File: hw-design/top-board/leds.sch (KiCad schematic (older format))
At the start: 30 parts

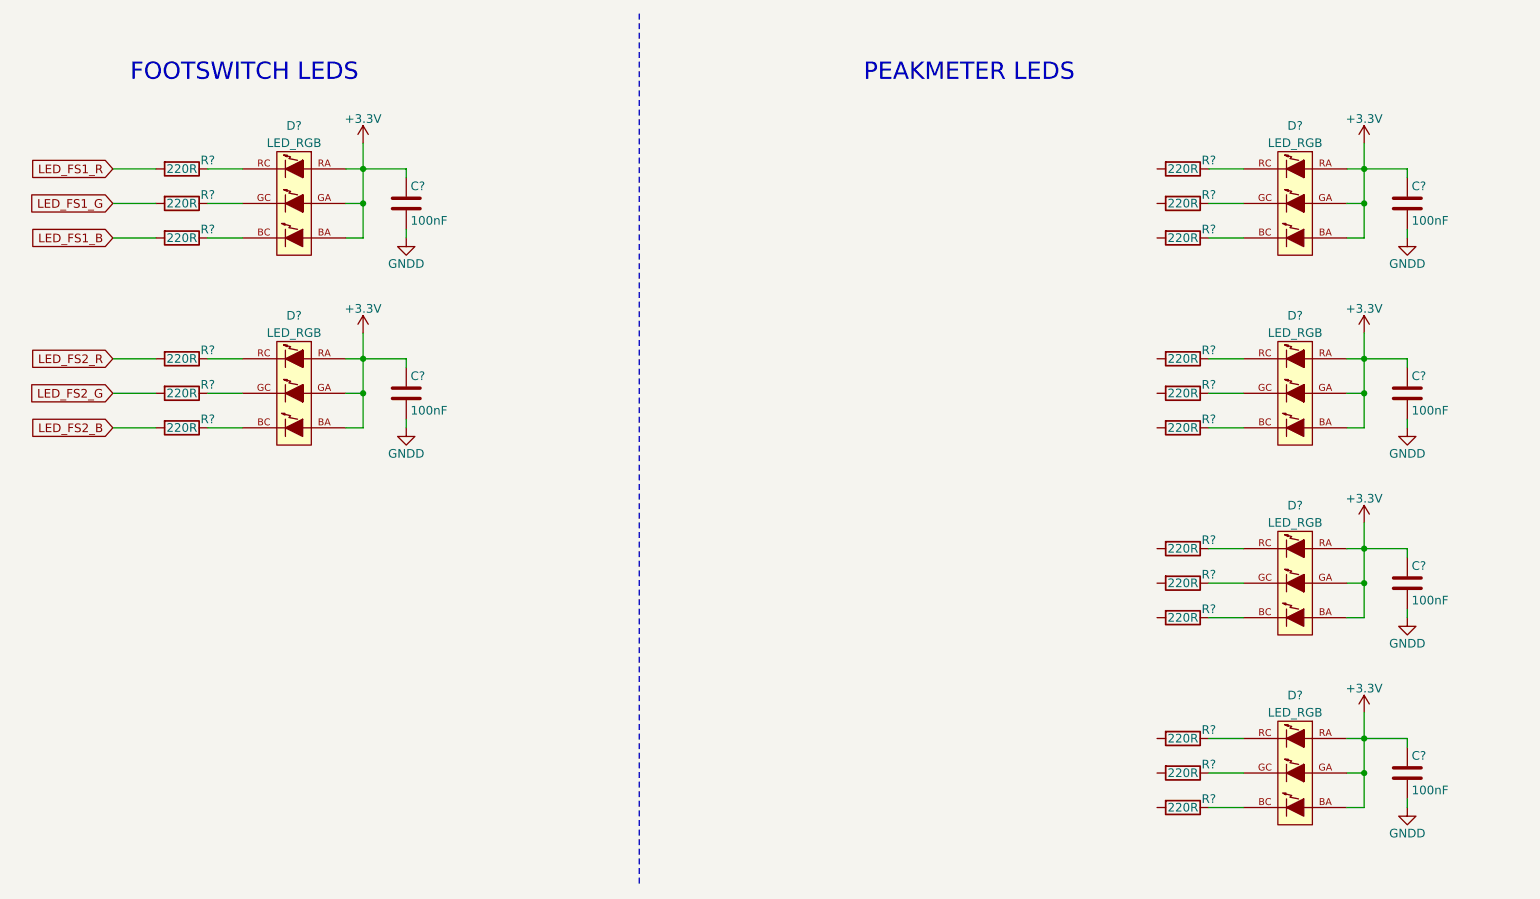
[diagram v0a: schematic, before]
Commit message: sch,top-board: added PCA9685 led driver
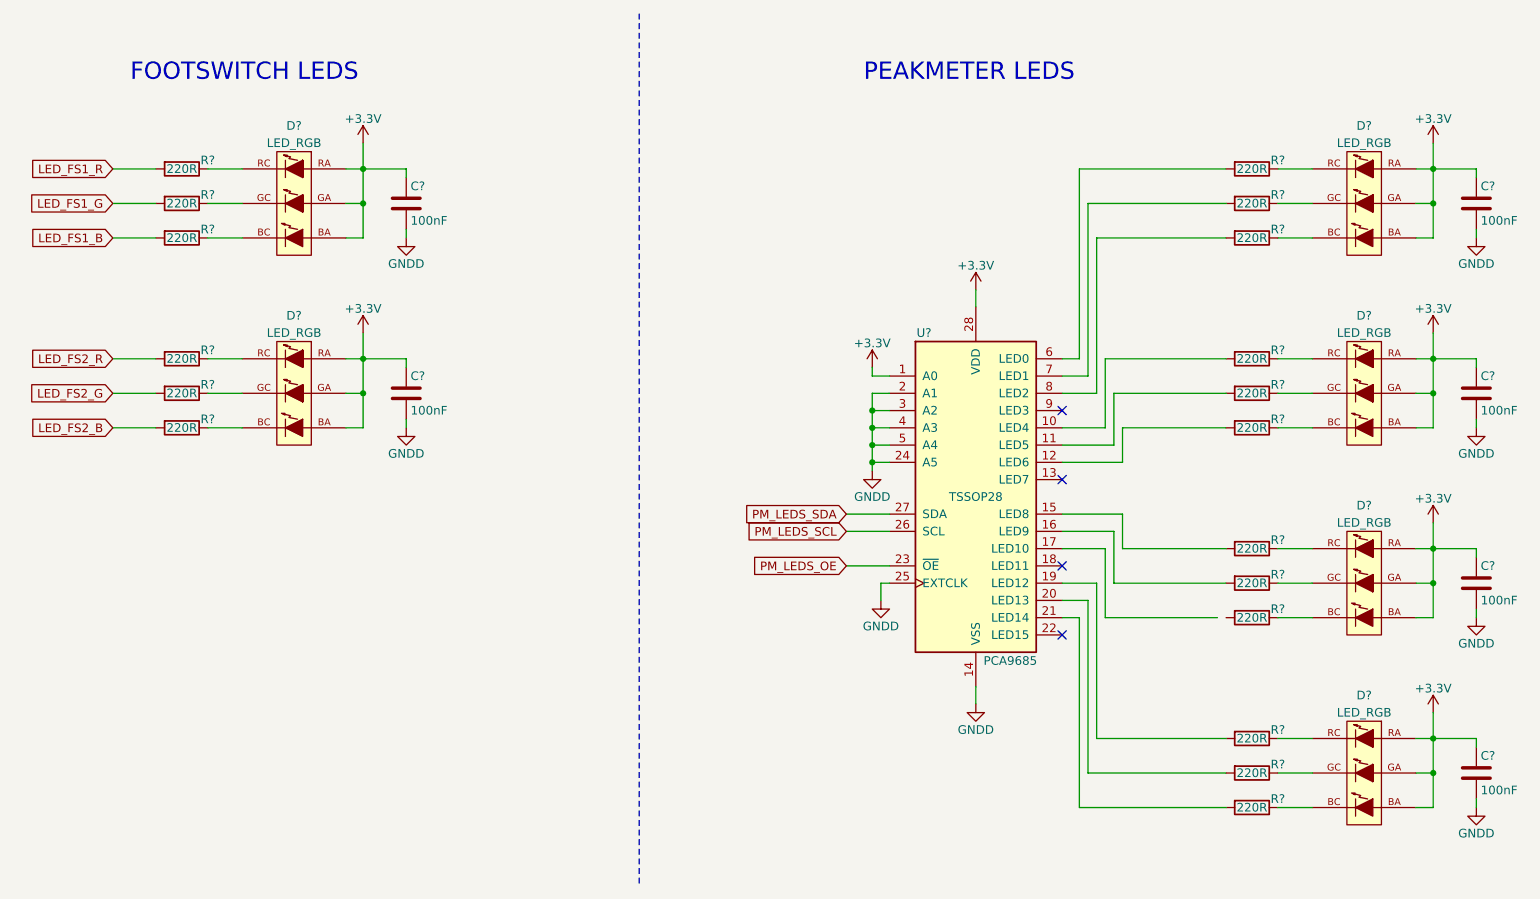
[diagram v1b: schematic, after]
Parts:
- added U?: PCA9685, TSSOP28, symbol PCA9685
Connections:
- net +3V3: now also U?.1 (A0), U?.28 (VDD)
- net GNDD: now also U?.14 (VSS), U?.2 (A1), U?.24 (A5), U?.25 (EXTCLK), U?.3 (A2), U?.4 (A3), U?.5 (A4)
- net at R?.2: now also U?.6 (LED0)
- net at R?.2: now also U?.7 (LED1)
- net at R?.2: now also U?.8 (LED2)
- net at R?.2: now also U?.10 (LED4)
- net at R?.2: now also U?.11 (LED5)
- net at R?.2: now also U?.12 (LED6)
- net at R?.2: now also U?.15 (LED8)
- net at R?.2: now also U?.16 (LED9)
- net at R?.2: now also U?.19 (LED12)
- net at R?.2: now also U?.20 (LED13)
- net at R?.2: now also U?.21 (LED14)
- new net PM_LEDS_OE: U?.23 (~OE~)
- new net PM_LEDS_SCL: U?.26 (SCL)
- new net PM_LEDS_SDA: U?.27 (SDA)
- no-connect marks 0 -> 4
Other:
- moved on the sheet: C?, D?, R?

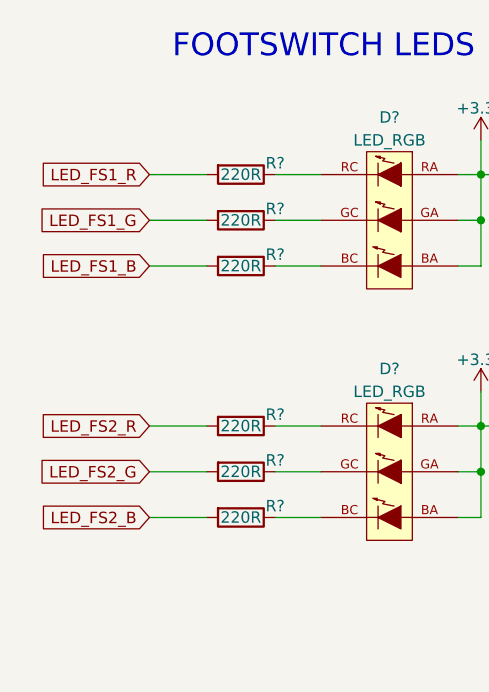
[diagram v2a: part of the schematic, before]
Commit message: sch,top-board: adding uC signals (wip)
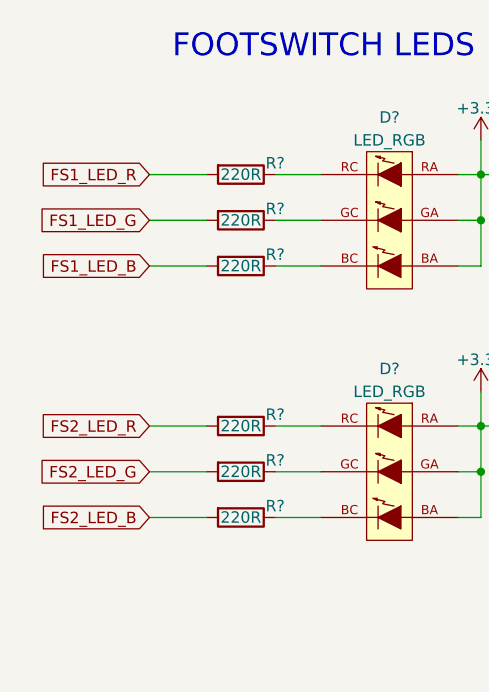
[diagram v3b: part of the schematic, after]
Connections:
- net LED_FS1_B renamed FS1_LED_B
- net LED_FS1_G renamed FS1_LED_G
- net LED_FS1_R renamed FS1_LED_R
- net LED_FS2_B renamed FS2_LED_B
- net LED_FS2_G renamed FS2_LED_G
- net LED_FS2_R renamed FS2_LED_R
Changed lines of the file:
@@
 	1    0    0    -1
 $EndComp
-Text GLabel 1750 1850 0    50   Input ~ 0
-LED_FS1_R
-Text GLabel 1750 2050 0    50   Input ~ 0
-LED_FS1_G
-Text GLabel 1750 2250 0    50   Input ~ 0
-LED_FS1_B
 $Comp
 L LED_RGB D?
@@
 	1    0    0    -1
 $EndComp
-Text GLabel 1750 2950 0    50   Input ~ 0
-LED_FS2_R
-Text GLabel 1750 3150 0    50   Input ~ 0
-LED_FS2_G
-Text GLabel 1750 3350 0    50   Input ~ 0
-LED_FS2_B
 Text Notes 1850 1350 0    100  ~ 0
 FOOTSWITCH LEDS
@@
 NoConn ~ 7250 4550
 NoConn ~ 7250 4150
+Text GLabel 1750 1850 0    50   Input ~ 0
+FS1_LED_R
+Text GLabel 1750 2050 0    50   Input ~ 0
+FS1_LED_G
+Text GLabel 1750 2250 0    50   Input ~ 0
+FS1_LED_B
+Text GLabel 1750 2950 0    50   Input ~ 0
+FS2_LED_R
+Text GLabel 1750 3150 0    50   Input ~ 0
+FS2_LED_G
+Text GLabel 1750 3350 0    50   Input ~ 0
+FS2_LED_B
 $EndSCHEMATC

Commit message: sch,top-board: annotation done
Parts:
- gave numbers to parts that had none: 31

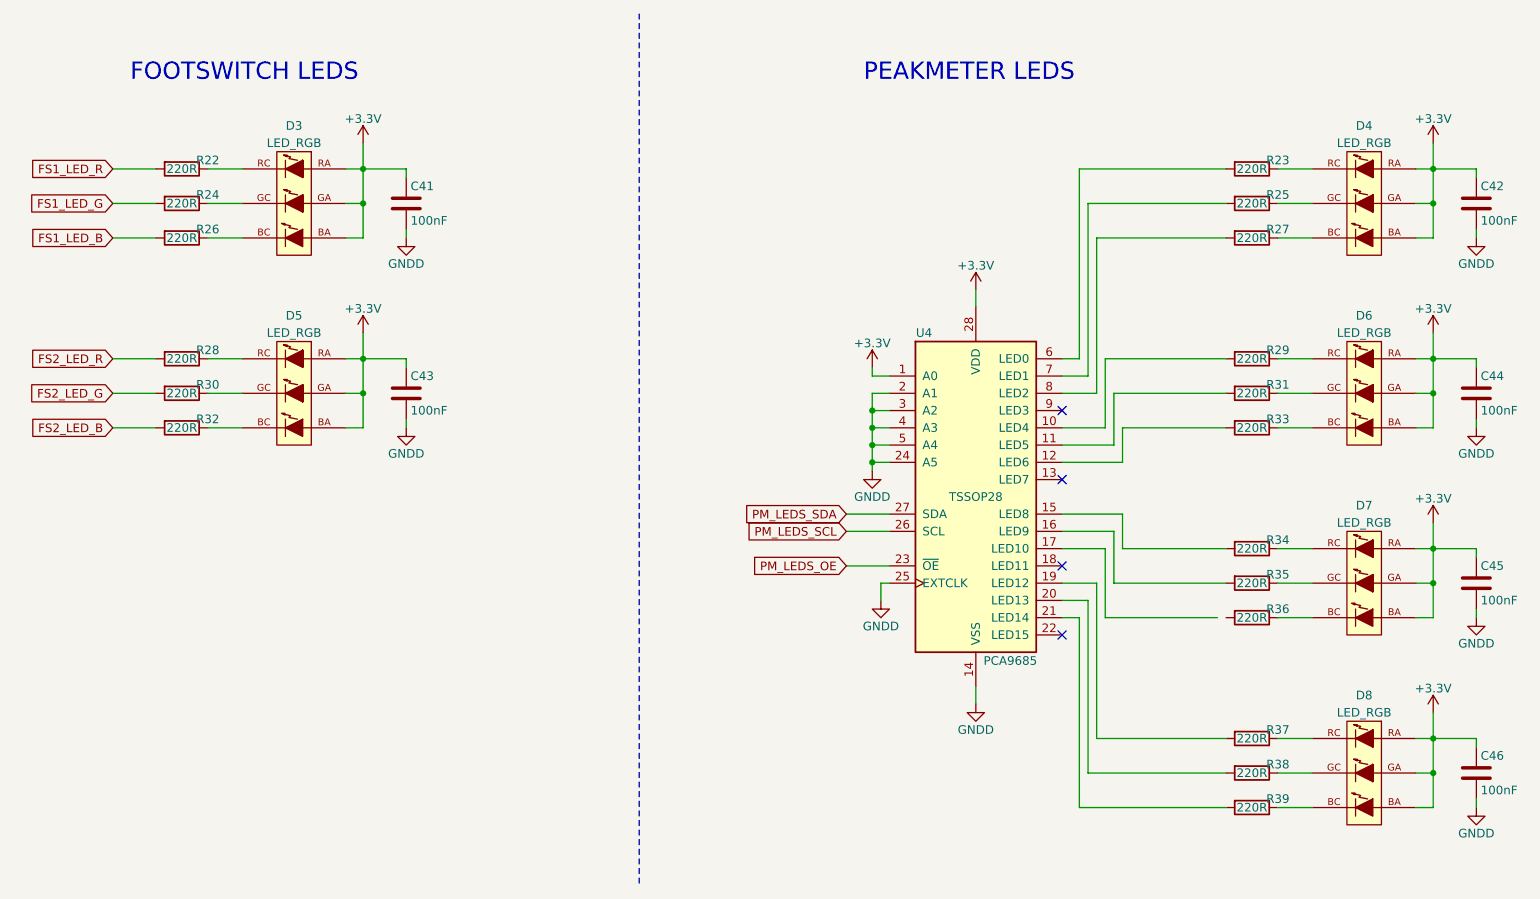
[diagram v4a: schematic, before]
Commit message: sch,top-board: fix signals names and unconnected wire
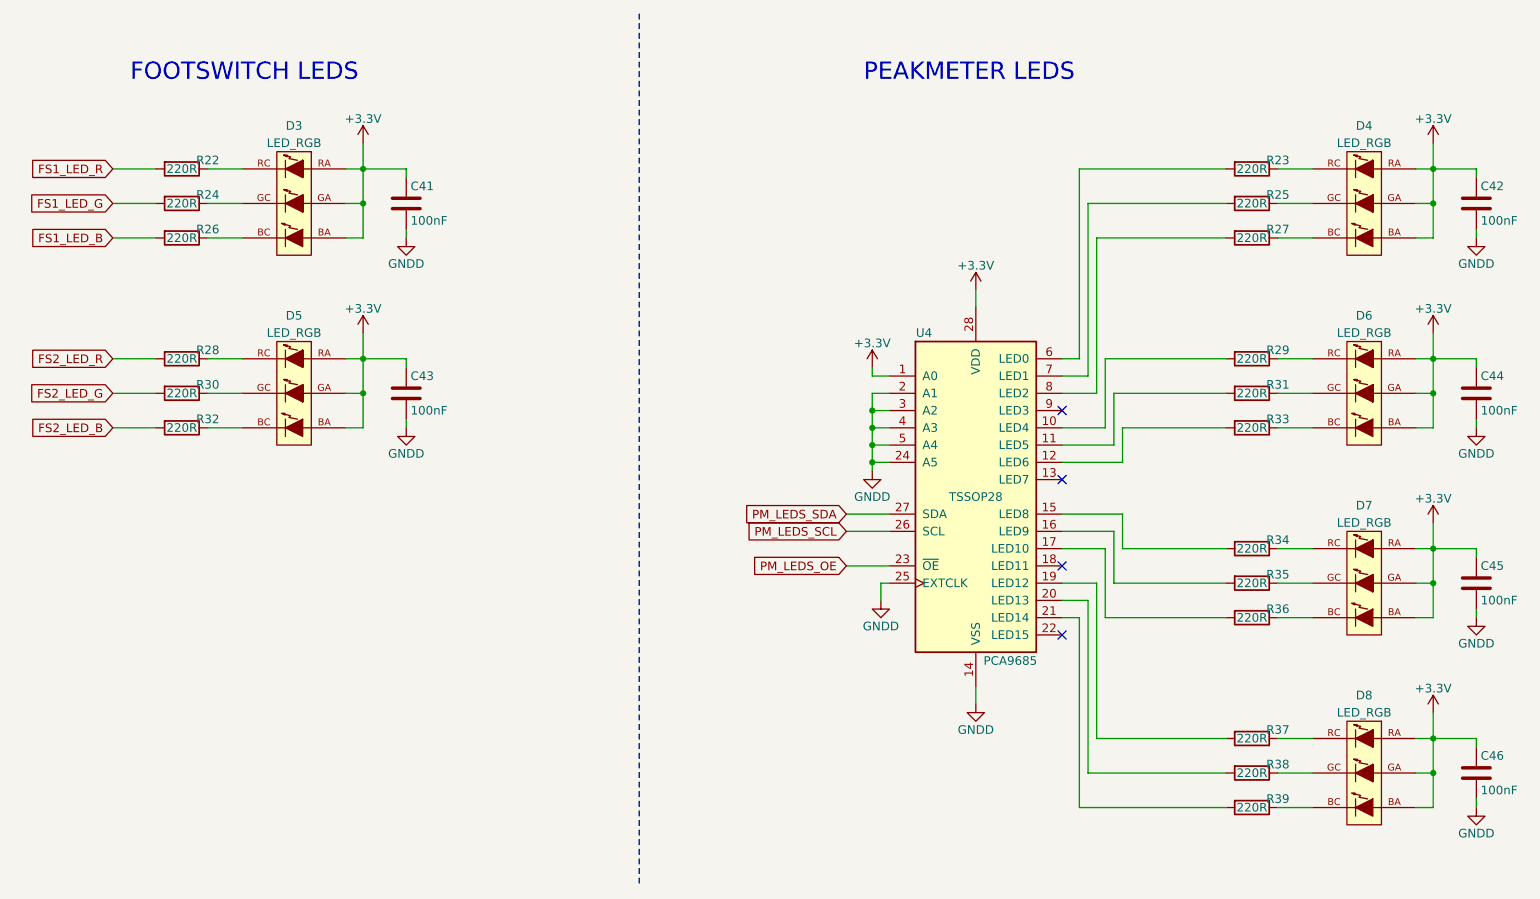
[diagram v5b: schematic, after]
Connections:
- net at R36.2: now also U4.17 (LED10)
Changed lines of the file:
@@
 	2500 2250 2300 2250
 Wire Wire Line
-	3200 1700 3200 2250
+	3200 1700 3200 1850
+Wire Wire Line
+	3200 1850 3200 2050
+Wire Wire Line
+	3200 2050 3200 2250
 Wire Wire Line
 	3200 2250 3100 2250
@@
 Connection ~ 3200 2050
 Wire Wire Line
-	3100 1850 3450 1850
+	3100 1850 3200 1850
+Wire Wire Line
+	3200 1850 3450 1850
 Connection ~ 3200 1850
 Wire Wire Line
@@
 	2500 3350 2300 3350
 Wire Wire Line
-	3200 2800 3200 3350
+	3200 2800 3200 2950
+Wire Wire Line
+	3200 2950 3200 3150
+Wire Wire Line
+	3200 3150 3200 3350
 Wire Wire Line
 	3200 3350 3100 3350
@@
 Connection ~ 3200 3150
 Wire Wire Line
-	3100 2950 3450 2950
+	3100 2950 3200 2950
+Wire Wire Line
+	3200 2950 3450 2950
 Connection ~ 3200 2950
 Wire Wire Line
@@
 Connection ~ 9400 5150
 Wire Wire Line
-	9300 5150 9650 5150
+	9300 5150 9400 5150
+Wire Wire Line
+	9400 5150 9650 5150
 Connection ~ 9400 5350
 Wire Wire Line
@@
 	9400 5550 9300 5550
 Wire Wire Line
-	9400 5000 9400 5550
+	9400 5000 9400 5150
+Wire Wire Line
+	9400 5150 9400 5350
+Wire Wire Line
+	9400 5350 9400 5550
 Wire Wire Line
 	8700 5550 8500 5550
@@
 Connection ~ 9400 4050
 Wire Wire Line
-	9300 4050 9650 4050
+	9300 4050 9400 4050
+Wire Wire Line
+	9400 4050 9650 4050
 Connection ~ 9400 4250
 Wire Wire Line
@@
 	9400 4450 9300 4450
 Wire Wire Line
-	9400 3900 9400 4450
+	9400 3900 9400 4050
+Wire Wire Line
+	9400 4050 9400 4250
+Wire Wire Line
+	9400 4250 9400 4450
 Wire Wire Line
 	8700 4450 8500 4450
@@
 Connection ~ 9400 2950
 Wire Wire Line
-	9300 2950 9650 2950
+	9300 2950 9400 2950
+Wire Wire Line
+	9400 2950 9650 2950
 Connection ~ 9400 3150
 Wire Wire Line
@@
 	9400 3350 9300 3350
 Wire Wire Line
-	9400 2800 9400 3350
+	9400 2800 9400 2950
+Wire Wire Line
+	9400 2950 9400 3150
+Wire Wire Line
+	9400 3150 9400 3350
 Wire Wire Line
 	8700 3350 8500 3350
@@
 Connection ~ 9400 1850
 Wire Wire Line
-	9300 1850 9650 1850
+	9300 1850 9400 1850
+Wire Wire Line
+	9400 1850 9650 1850
 Connection ~ 9400 2050
 Wire Wire Line
@@
 	9400 2250 9300 2250
 Wire Wire Line
-	9400 1700 9400 2250
+	9400 1700 9400 1850
+Wire Wire Line
+	9400 1850 9400 2050
+Wire Wire Line
+	9400 2050 9400 2250
 Wire Wire Line
 	8700 2250 8500 2250
@@
 	7550 4250 8200 4250
 Wire Wire Line
-	8150 4450 7500 4450
+	8200 4450 7500 4450
 Wire Wire Line
 	7500 4450 7500 4050
@@
 	6250 3150 6150 3150
 Wire Wire Line
-	6150 3150 6150 3600
+	6150 3150 6150 3250
+Wire Wire Line
+	6150 3250 6150 3350
+Wire Wire Line
+	6150 3350 6150 3450
+Wire Wire Line
+	6150 3450 6150 3550
+Wire Wire Line
+	6150 3550 6150 3600
 $Comp
 L +3.3V #PWR76

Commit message: sch,top-board: DRC passing
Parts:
- renumbered R22 to R24, R23 to R25, R24 to R26, R25 to R27, R26 to R28, R27 to R29, R28 to R30, R29 to R31, R30 to R32, R31 to R33, R32 to R34, R33 to R35, R34 to R36, R35 to R37, R36 to R38, R37 to R39, R38 to R40, R39 to R41

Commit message: sch,top-board: BOM added
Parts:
- C41, C42, C43, C44, C45, C46: MPN (none) -> C1608X7R1E104K080AA
- R24, R25, R26, R27, R28, R29, R30, R31, R32, R33, R34, R35, R36, R37, R38, R39, R40, R41: MPN (none) -> RMCF0603JT220R
- U4: MPN (none) -> PCA9685PW,112
